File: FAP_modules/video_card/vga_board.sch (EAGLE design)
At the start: 31 parts, among them IC1 IS61LV256, IC2 IS61LV256

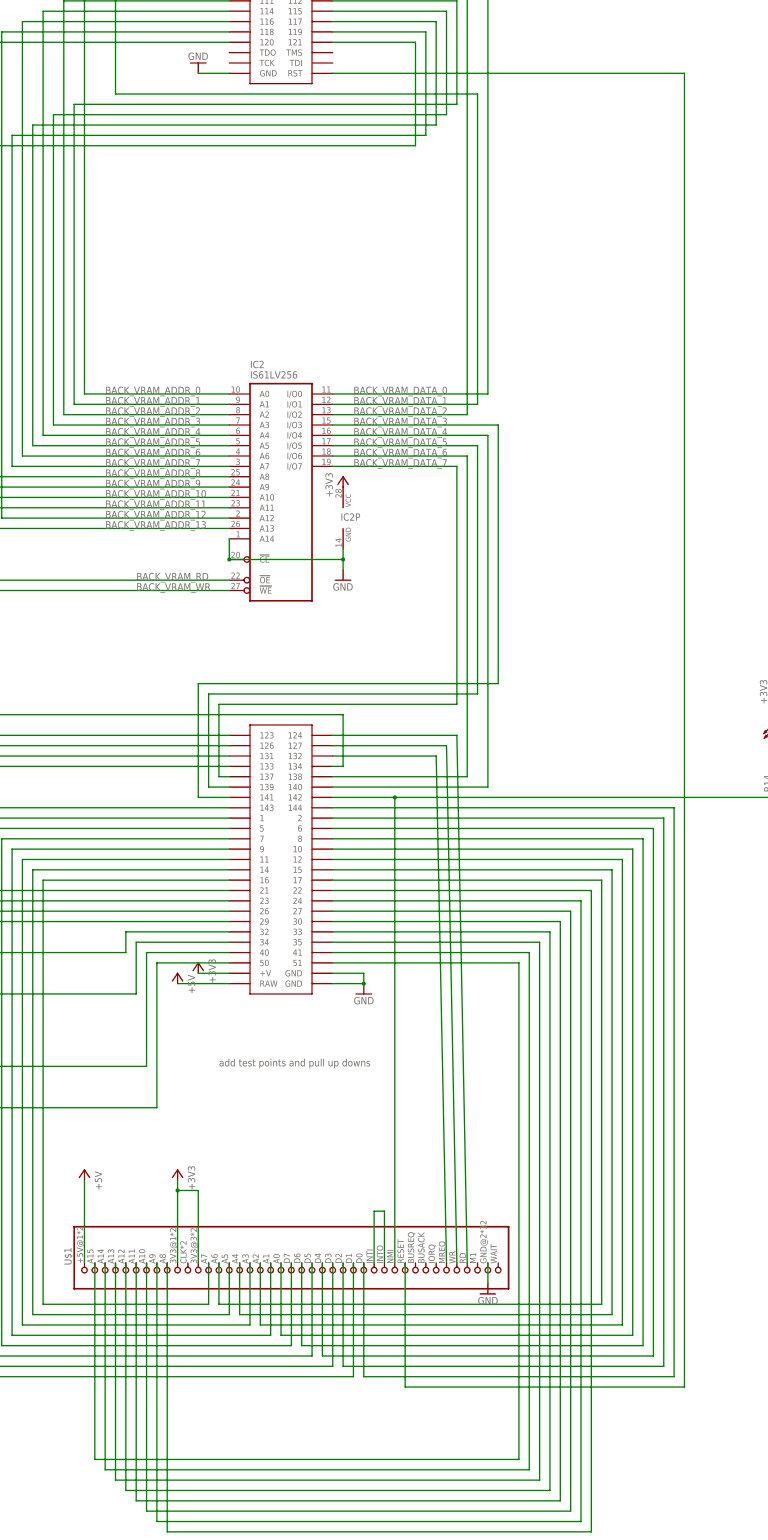
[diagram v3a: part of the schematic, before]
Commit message: added all Z80 signals on bus
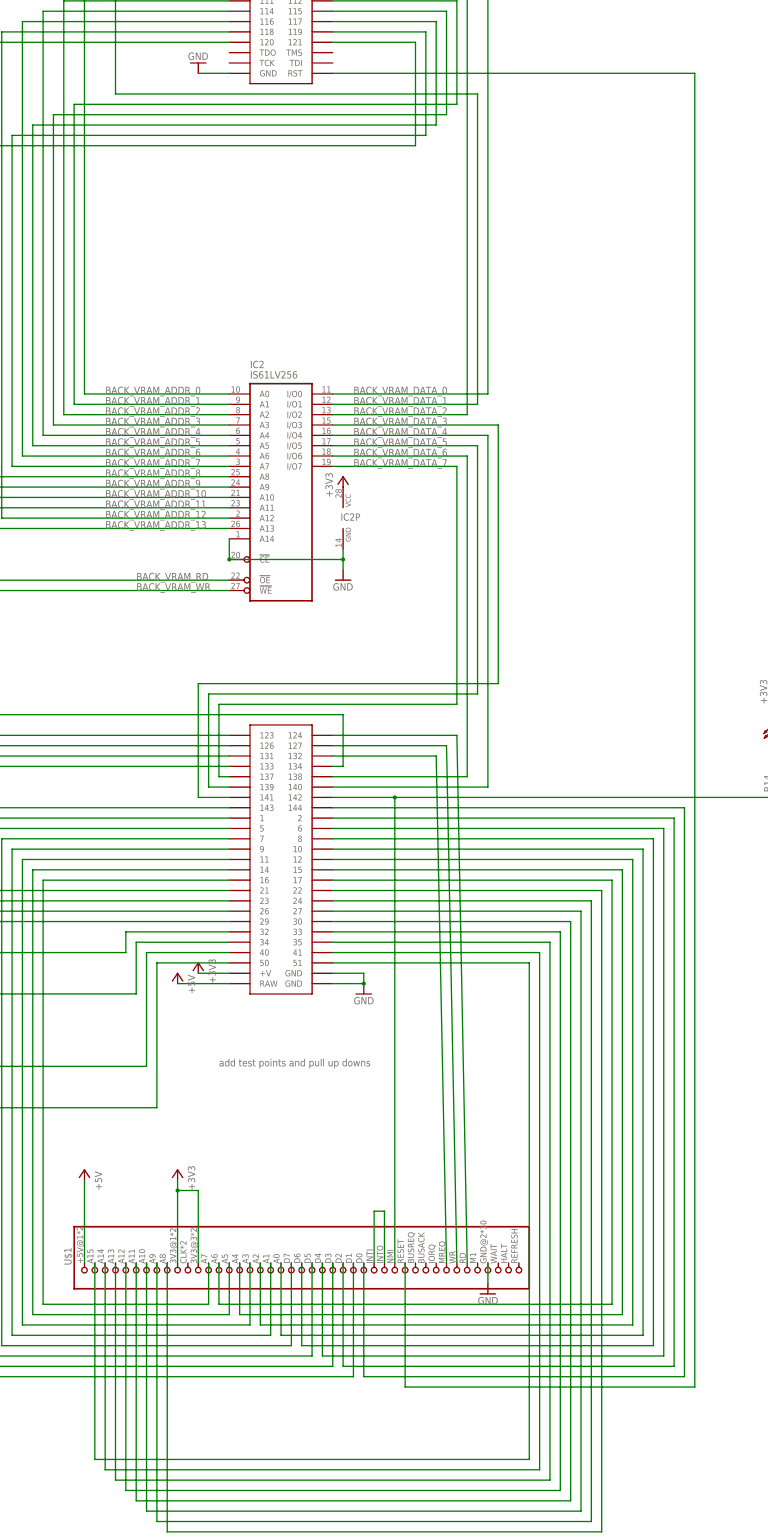
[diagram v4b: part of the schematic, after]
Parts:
- U$1: value FAP_BUS_FAP_BUS -> FAP_BUS; device cpu_board:FAP_BUS_FAP_BUS -> fap_bus:FAP_BUS

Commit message: board cleanup
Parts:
- added JP1: JUMPER-PAD-2-NO, SparkFun-Passives:JUMPER-PAD-2-NO
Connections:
- new net N$39: JP1.1, U$1.30
- net N$36: now also JP1.2; no longer U$1.30
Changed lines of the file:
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@@
 <part name="+3V11" library="supply1" deviceset="+3V3" device=""/>
 <part name="+3V12" library="supply1" deviceset="+3V3" device=""/>
+<part name="JP1" library="SparkFun-Passives" deviceset="JUMPER-PAD-2-NO" device=""/>
 </parts>
 <sheets>
@@
 <instance part="+3V11" gate="G$1" x="-510.54" y="193.04"/>
 <instance part="+3V12" gate="G$1" x="-274.32" y="-104.14"/>
+<instance part="JP1" gate="G$1" x="-368.3" y="-218.44" rot="R90"/>
 </instances>
 <busses>
@@
 <pinref part="U$3" gate="G$2" pin="142"/>
 <wire x1="-383.54" y1="-132.08" x2="-368.3" y2="-132.08" width="0.1524" layer="91"/>
+<pinref part="R14" gate="G$1" pin="1"/>
+<pinref part="JP1" gate="G$1" pin="2"/>
 <wire x1="-368.3" y1="-132.08" x2="-274.32" y2="-132.08" width="0.1524" layer="91"/>
-<pinref part="U$1" gate="G$1" pin="30"/>
-<wire x1="-368.3" y1="-246.38" x2="-368.3" y2="-132.08" width="0.1524" layer="91"/>
+<wire x1="-368.3" y1="-213.36" x2="-368.3" y2="-132.08" width="0.1524" layer="91"/>
 <junction x="-368.3" y="-132.08"/>
-<pinref part="R14" gate="G$1" pin="1"/>
 </segment>
 </net>
@@
 </segment>
 </net>
+<net name="N$39" class="0">
+<segment>
+<pinref part="U$1" gate="G$1" pin="30"/>
+<pinref part="JP1" gate="G$1" pin="1"/>
+<wire x1="-368.3" y1="-223.52" x2="-368.3" y2="-246.38" width="0.1524" layer="91"/>
+</segment>
+</net>
